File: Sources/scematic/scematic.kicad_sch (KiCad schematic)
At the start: 19 parts, among them u1 ADC 1, u2 ADC 2, u3 ADC 3, u4 ADC 4, u5 ADC 5

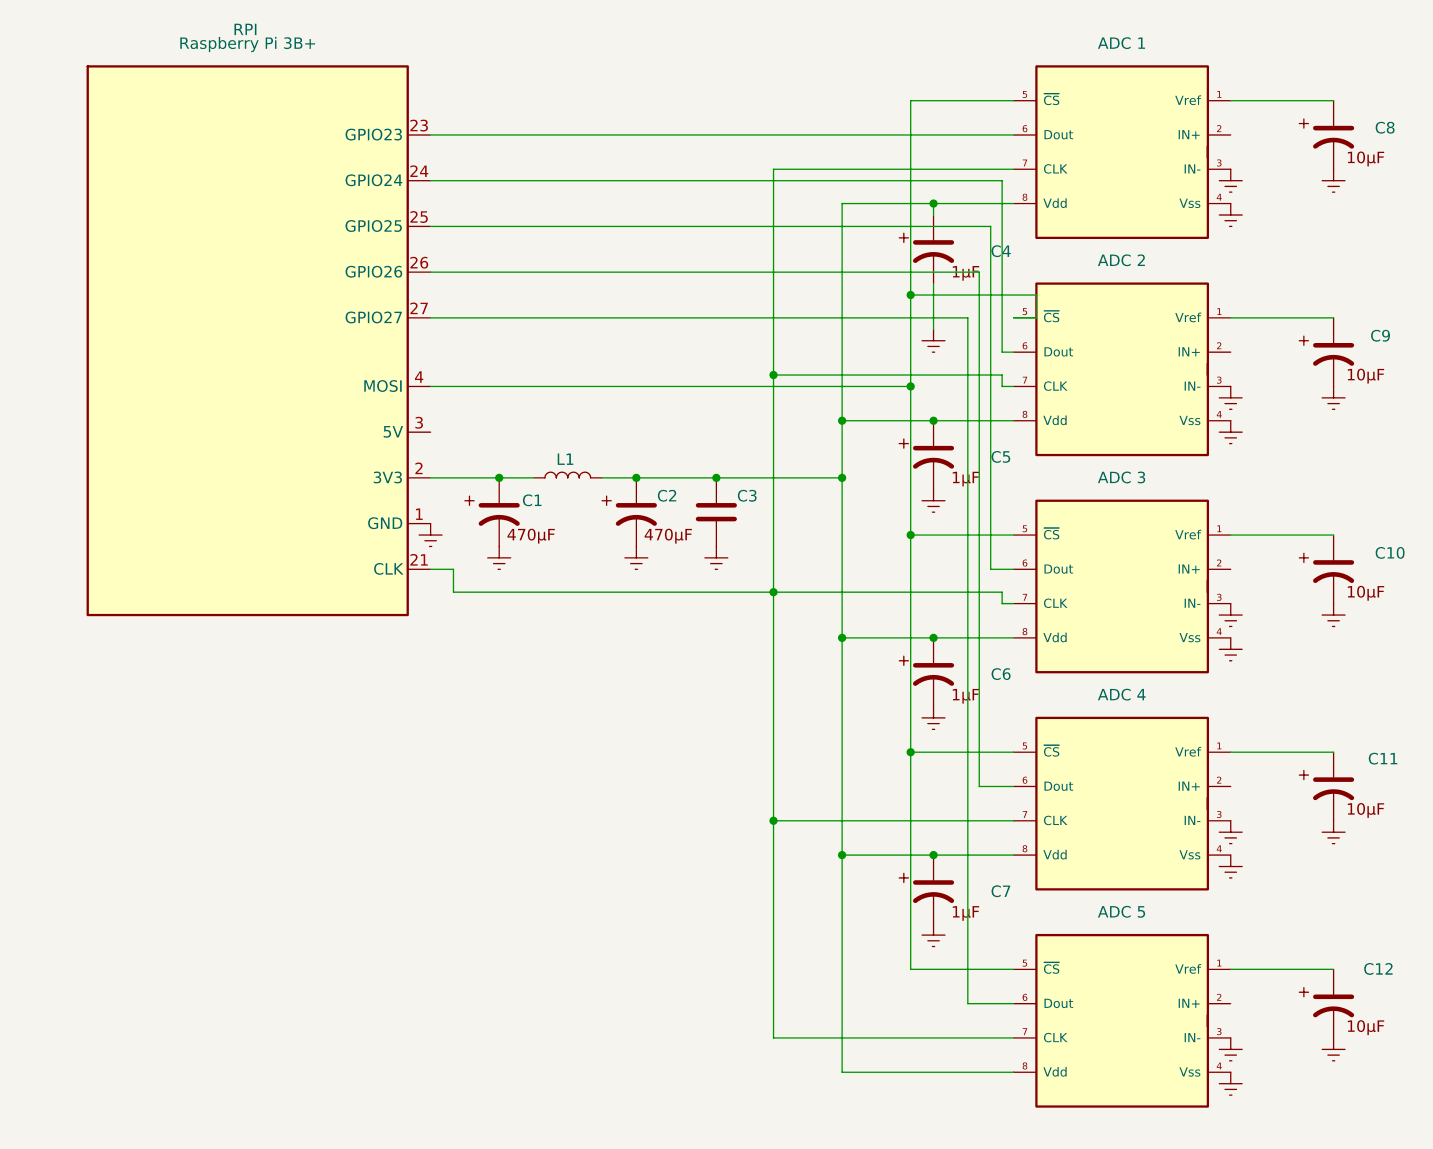
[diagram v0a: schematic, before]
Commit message: scematic and blokkdiagrams updated
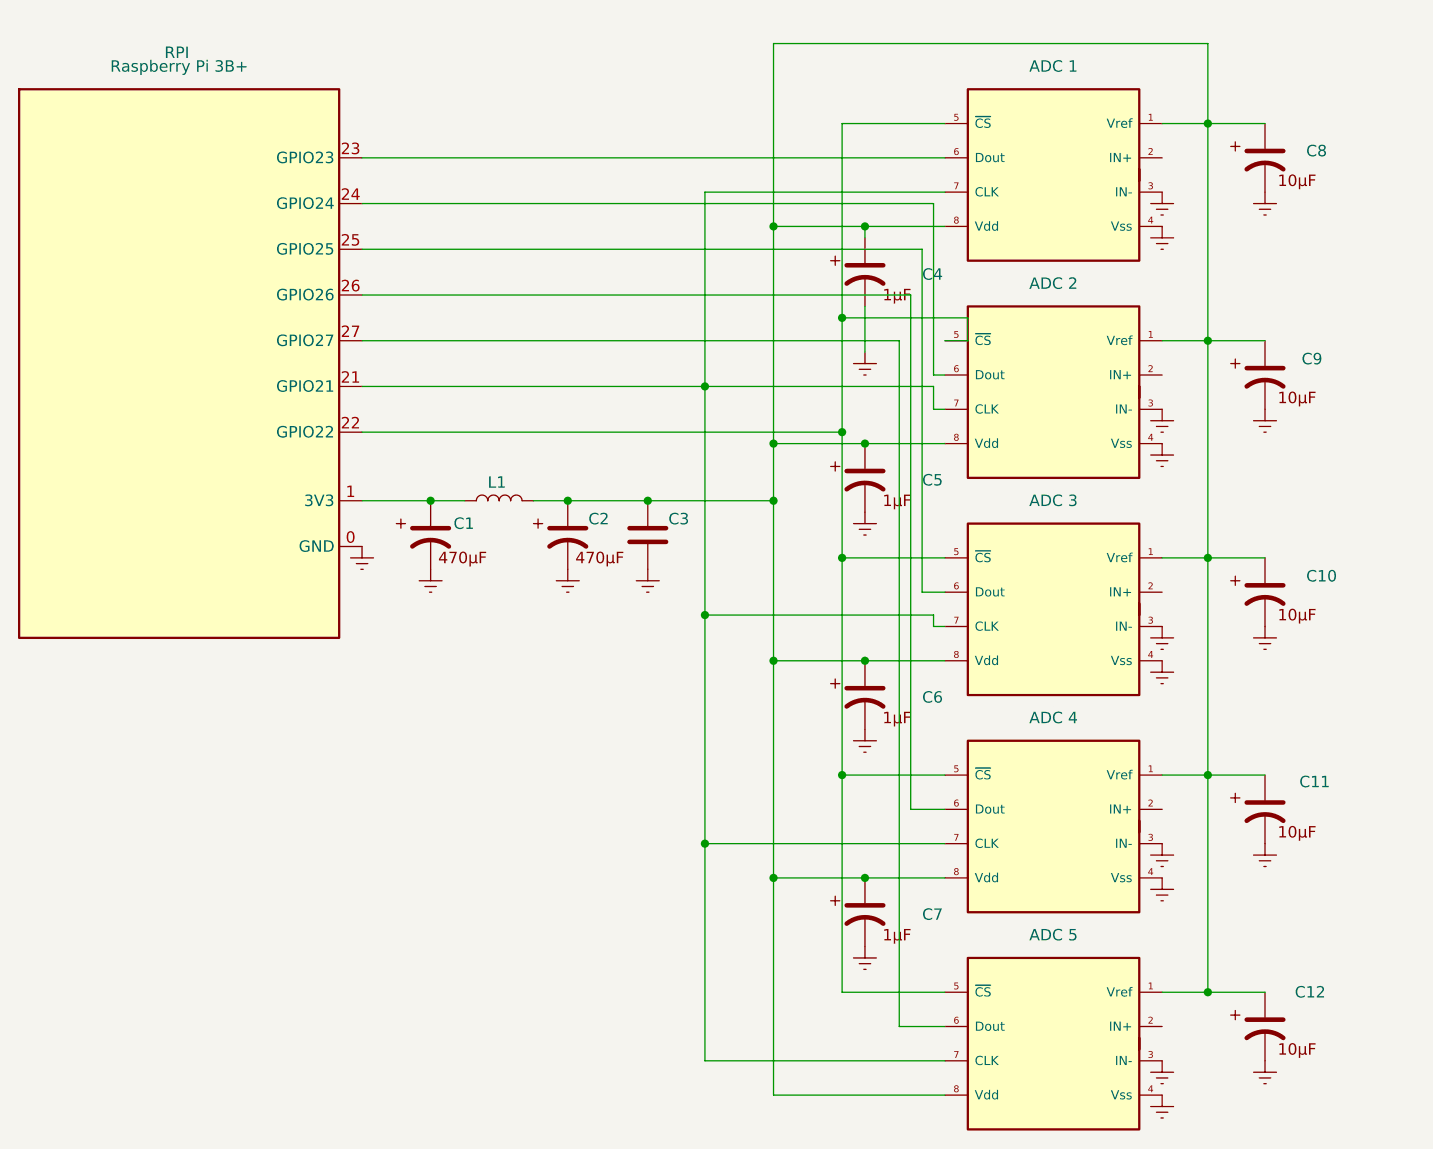
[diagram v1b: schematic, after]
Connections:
- net GNDREF: now also RPI.0 (GND); no longer RPI.1 (GND)
- net at C12., u5.1 (Vref): now also C10., C11., C2., C3.1, C4., C5., C6., C7., C8., C9., L1.2, u1.1 (Vref), u1.8 (Vdd), u2.1 (Vref), u2.8 (Vdd), u3.1 (Vref), u3.8 (Vdd), u4.1 (Vref), u4.8 (Vdd), u5.8 (Vdd)
- net at u1.5 (~{CS}), u2.5 (~{CS}), u3.5 (~{CS})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: now also RPI.22 (GPIO22); no longer RPI.4 (MOSI)
- new net: C1., L1.1, RPI.1 (3V3)
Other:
- moved on the sheet: C1, C10, C11, C12, C2, C3, C4, C5, C6, C7, C8, C9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
